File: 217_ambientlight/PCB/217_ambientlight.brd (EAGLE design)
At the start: 27.9 x 39.4 mm, 8 parts

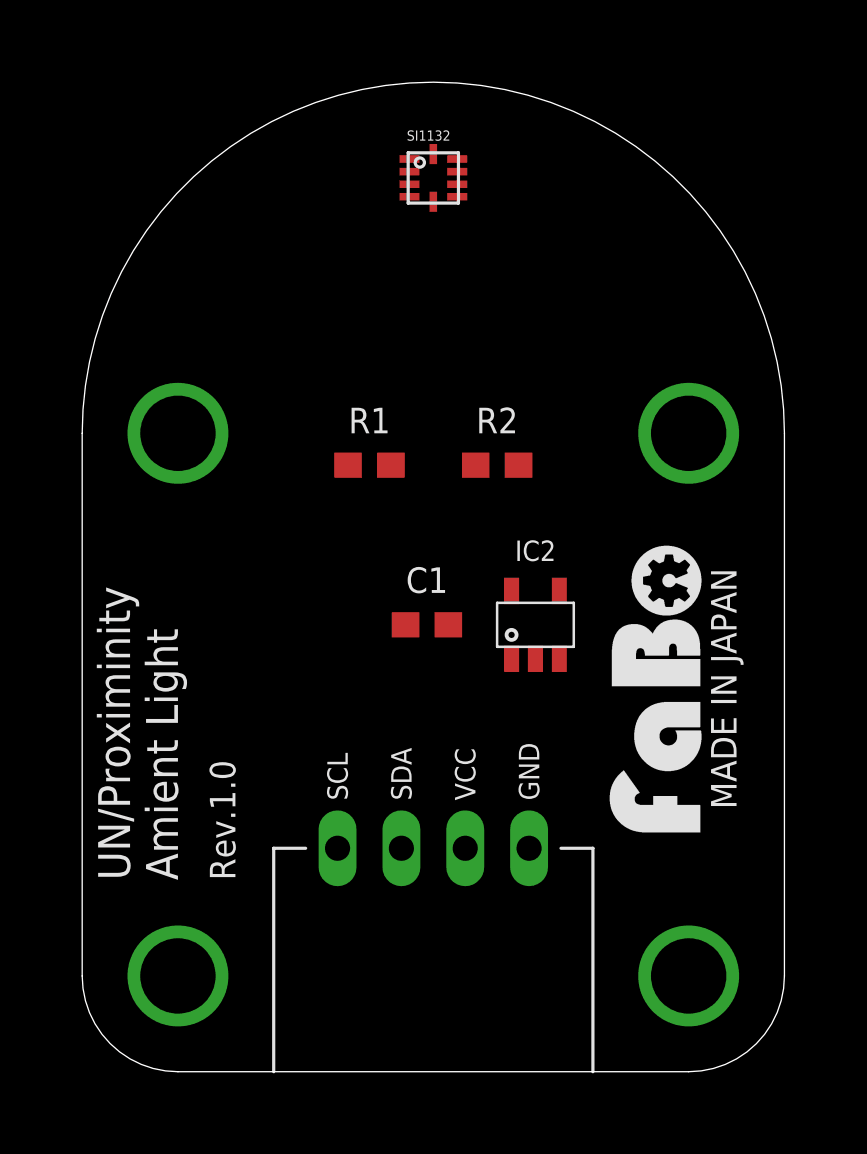
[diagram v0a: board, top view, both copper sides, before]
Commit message: Add new sensors
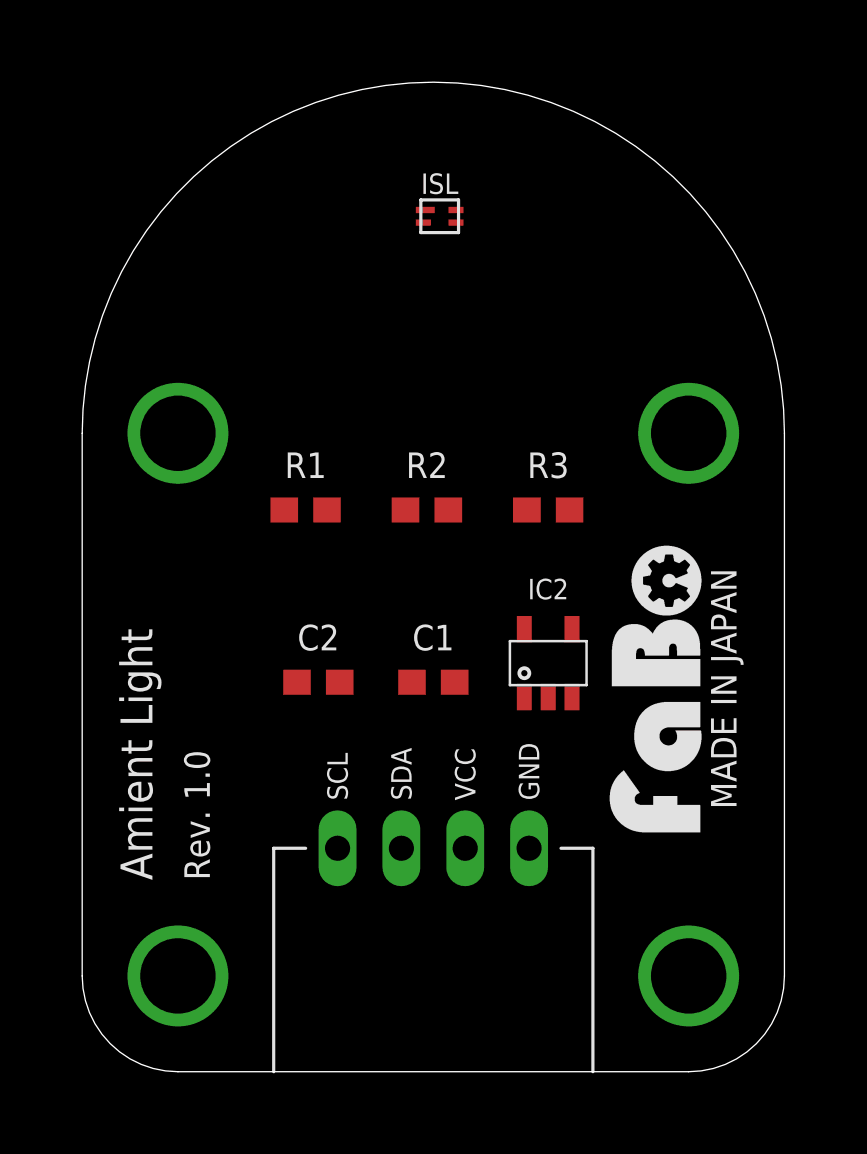
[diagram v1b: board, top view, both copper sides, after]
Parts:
- removed SI1132: SL-SI1132, FaBo-Mems:SILICONLABS-SI1132
- added C2: 1uF, GClue:EIA0603
- added ISL: IN-ISL29034, FaBo-Mems:INTERSIL-ISL29034
- added R3: 100, GClue:EIA0603
- moved R2 3.31 mm to (13.7, 22.4)
- moved R1 3.10 mm to (8.89, 22.4)
- moved C1 2.30 mm to (14.0, 15.5)
- moved IC2 1.61 mm to (18.5, 16.3)
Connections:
- new net N$1: C2.1, ISL.1, R3.1
- net 3V3: now also R3.2; no longer SI1132.3, SI1132.6, SI1132.7, SI1132.9
- net GND: now also C2.2, ISL.2; no longer SI1132.8
- net SCL: now also ISL.3; no longer SI1132.2
- net SDA: now also ISL.4; no longer SI1132.1
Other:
- board text added: "Amient Light"
- board text added: "Rev. 1.0"
- board text removed: "Rev.1.0"
- board text removed: "UN/Proximinity Amient Light"
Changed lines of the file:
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@@
 <plain>
 <text x="26.035" y="15.24" size="1.016" layer="21" font="vector" ratio="12" rot="R90" align="bottom-center">MADE IN JAPAN</text>
-<text x="3.81" y="7.62" size="1.27" layer="21" font="vector" ratio="12" rot="R90">UN/Proximinity
-Amient Light</text>
-<text x="6.096" y="7.62" size="1.016" layer="21" font="vector" ratio="12" rot="R90">Rev.1.0</text>
+<text x="2.794" y="7.62" size="1.27" layer="21" font="vector" ratio="12" rot="R90">Amient Light</text>
+<text x="5.08" y="7.62" size="1.016" layer="21" font="vector" ratio="12" rot="R90">Rev. 1.0</text>
 </plain>
 <attributes>
@@
 <element name="U$3" library="FaBo" package="LOGO_FABO_M" value="" x="24.638" y="15.24" rot="R90"/>
 <element name="U$4" library="GClue" package="LOGO_OSHW_T_M_BOTTOM" value="" x="13.97" y="5.08"/>
-<element name="R1" library="GClue" package="EIA0603" value="4.7k" x="11.43" y="24.13"/>
-<element name="R2" library="GClue" package="EIA0603" value="4.7k" x="16.51" y="24.13"/>
-<element name="SI1132" library="FaBo-Mems" package="SILICONLABS-SI1132" value="SL-SI1132" x="13.97" y="35.56"/>
-<element name="IC2" library="FaBo-Supply" package="TI-LP2985" value="" x="18.034" y="17.78"/>
-<element name="C1" library="GClue" package="EIA0603" value="1uF" x="13.716" y="17.78"/>
+<element name="R1" library="GClue" package="EIA0603" value="4.7k" x="8.89" y="22.352"/>
+<element name="R2" library="GClue" package="EIA0603" value="4.7k" x="13.716" y="22.352"/>
+<element name="ISL" library="FaBo-Mems" package="INTERSIL-ISL29034" value="IN-ISL29034" x="14.224" y="34.036"/>
+<element name="R3" library="GClue" package="EIA0603" value="100" x="18.542" y="22.352"/>
+<element name="C2" library="GClue" package="EIA0603" value="1uF" x="9.398" y="15.494"/>
+<element name="IC2" library="FaBo-Supply" package="TI-LP2985" value="" x="18.542" y="16.256"/>
+<element name="C1" library="GClue" package="EIA0603" value="1uF" x="13.97" y="15.494"/>
 </elements>
 <signals>
@@
 <contactref element="R1" pad="2"/>
 <contactref element="R2" pad="2"/>
-<contactref element="SI1132" pad="3"/>
-<contactref element="SI1132" pad="7"/>
-<contactref element="SI1132" pad="6"/>
-<contactref element="SI1132" pad="9"/>
+<contactref element="R3" pad="2"/>
 <contactref element="IC2" pad="5"/>
 <contactref element="C1" pad="1"/>
-<wire x1="14.92" y1="35.312" x2="14.92" y2="36.312" width="0" layer="19" extent="1-1"/>
-<wire x1="14.92" y1="34.812" x2="14.92" y2="35.312" width="0" layer="19" extent="1-1"/>
-<wire x1="13.02" y1="35.312" x2="14.92" y2="35.312" width="0" layer="19" extent="1-1"/>
-<wire x1="17.36" y1="24.13" x2="14.92" y2="34.812" width="0" layer="19" extent="1-1"/>
-<wire x1="12.28" y1="24.13" x2="17.36" y2="24.13" width="0" layer="19" extent="1-1"/>
-<wire x1="17.084" y1="19.13" x2="12.28" y2="24.13" width="0" layer="19" extent="1-1"/>
-<wire x1="12.866" y1="17.78" x2="17.084" y2="19.13" width="0" layer="19" extent="1-1"/>
+<wire x1="14.566" y1="22.352" x2="19.392" y2="22.352" width="0" layer="19" extent="1-1"/>
+<wire x1="9.74" y1="22.352" x2="14.566" y2="22.352" width="0" layer="19" extent="1-1"/>
+<wire x1="17.592" y1="17.606" x2="19.392" y2="22.352" width="0" layer="19" extent="1-1"/>
+<wire x1="13.12" y1="15.494" x2="17.592" y2="17.606" width="0" layer="19" extent="1-1"/>
 </signal>
 <signal name="GND">
 <contactref element="J1" pad="GND"/>
-<contactref element="SI1132" pad="8"/>
+<contactref element="ISL" pad="2"/>
+<contactref element="C2" pad="2"/>
 <contactref element="IC2" pad="2"/>
 <contactref element="C1" pad="2"/>
-<wire x1="17.78" y1="8.89" x2="14.92" y2="35.812" width="0" layer="19" extent="1-1"/>
-<wire x1="18.034" y1="16.43" x2="17.78" y2="8.89" width="0" layer="19" extent="1-1"/>
-<wire x1="14.566" y1="17.78" x2="18.034" y2="16.43" width="0" layer="19" extent="1-1"/>
+<wire x1="10.248" y1="15.494" x2="13.574" y2="33.786" width="0" layer="19" extent="1-1"/>
+<wire x1="18.542" y1="14.906" x2="10.248" y2="15.494" width="0" layer="19" extent="1-1"/>
+<wire x1="17.78" y1="8.89" x2="18.542" y2="14.906" width="0" layer="19" extent="1-1"/>
+<wire x1="14.82" y1="15.494" x2="17.78" y2="8.89" width="0" layer="19" extent="1-1"/>
 </signal>
 <signal name="SCL">
 <contactref element="J1" pad="SCL"/>
 <contactref element="R2" pad="1"/>
-<contactref element="SI1132" pad="2"/>
-<wire x1="10.16" y1="8.89" x2="15.66" y2="24.13" width="0" layer="19" extent="1-1"/>
-<wire x1="13.02" y1="35.812" x2="10.16" y2="8.89" width="0" layer="19" extent="1-1"/>
+<contactref element="ISL" pad="3"/>
+<wire x1="10.16" y1="8.89" x2="12.866" y2="22.352" width="0" layer="19" extent="1-1"/>
+<wire x1="14.874" y1="33.786" x2="10.16" y2="8.89" width="0" layer="19" extent="1-1"/>
 </signal>
 <signal name="SDA">
 <contactref element="J1" pad="SDA"/>
 <contactref element="R1" pad="1"/>
-<contactref element="SI1132" pad="1"/>
-<wire x1="12.7" y1="8.89" x2="10.58" y2="24.13" width="0" layer="19" extent="1-1"/>
-<wire x1="13.02" y1="36.312" x2="12.7" y2="8.89" width="0" layer="19" extent="1-1"/>
+<contactref element="ISL" pad="4"/>
+<wire x1="12.7" y1="8.89" x2="8.04" y2="22.352" width="0" layer="19" extent="1-1"/>
+<wire x1="14.874" y1="34.286" x2="12.7" y2="8.89" width="0" layer="19" extent="1-1"/>
+</signal>
+<signal name="N$1">
+<contactref element="ISL" pad="1"/>
+<contactref element="R3" pad="1"/>
+<contactref element="C2" pad="1"/>
+<wire x1="17.692" y1="22.352" x2="8.548" y2="15.494" width="0" layer="19" extent="1-1"/>
+<wire x1="13.649" y1="34.286" x2="17.692" y2="22.352" width="0" layer="19" extent="1-1"/>
 </signal>
 <signal name="5V">
@@
 <contactref element="IC2" pad="1"/>
 <contactref element="J1" pad="VCC"/>
-<wire x1="18.984" y1="16.43" x2="15.24" y2="8.89" width="0" layer="19" extent="1-1"/>
-<wire x1="17.084" y1="16.43" x2="18.984" y2="16.43" width="0" layer="19" extent="1-1"/>
+<wire x1="19.492" y1="14.906" x2="15.24" y2="8.89" width="0" layer="19" extent="1-1"/>
+<wire x1="17.592" y1="14.906" x2="19.492" y2="14.906" width="0" layer="19" extent="1-1"/>
 </signal>
 </signals>
@@
 </board>
 </drawing>
-<compatibility>
-<note version="6.3" minversion="6.2.2" severity="warning">
-Since Version 6.2.2 text objects can contain more than one line,
-which will not be processed correctly with this version.
-</note>
-</compatibility>
 </eagle>

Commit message: fix 206_uv fix 217_ambientlight
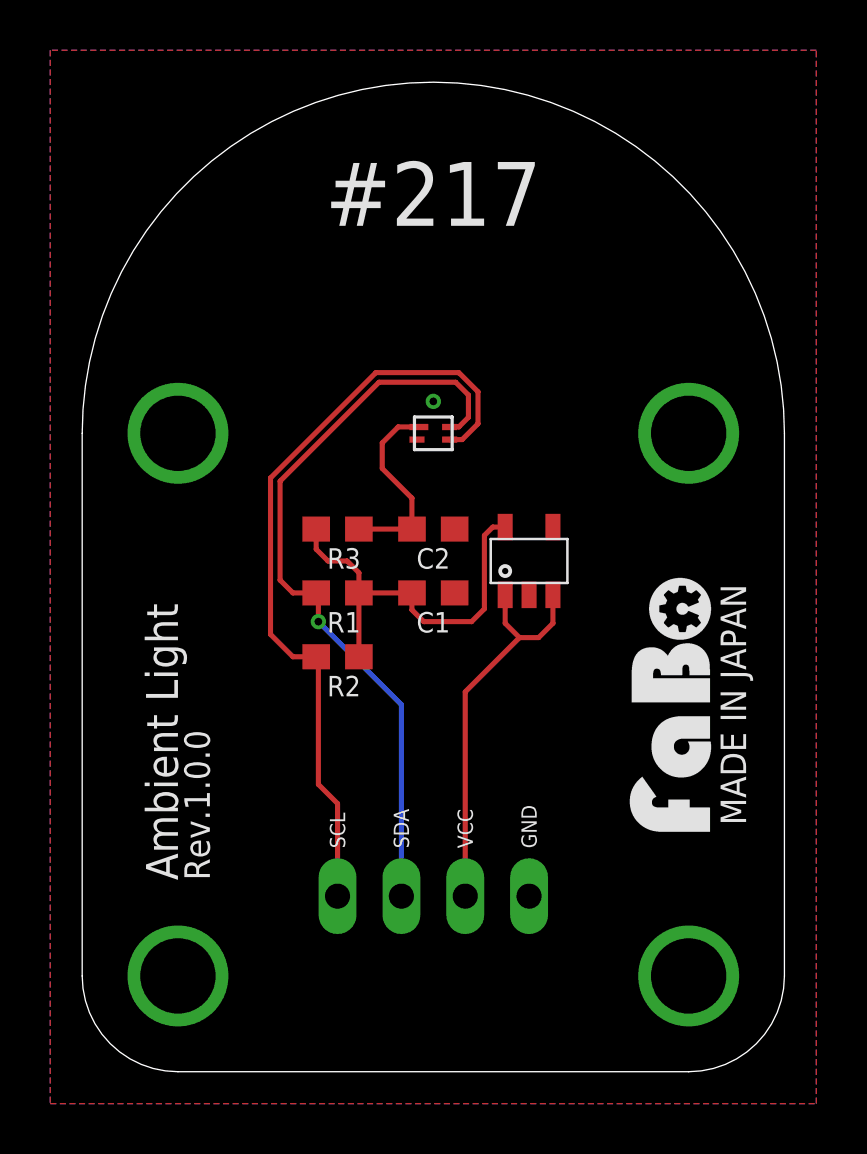
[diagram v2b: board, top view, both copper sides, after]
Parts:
- removed ISL: IN-ISL29034, FaBo-Mems:INTERSIL-ISL29034
- removed U$4: (no value), GClue:LOGO_OSHW_T_M_BOTTOM
- added IC1: (no value), FaBo-Supply:TI-LP2985
- added U$2: (no value), FaBo-etc:LOGO_OSHW_T_MS_BOTTOM
- C1, C2: device GClue:EIA0603 -> FaBo-Capacitor:0603
- IC2: value (none) -> IN-ISL29034; device FaBo-Supply:TI-LP2985 -> FaBo-Mems:INTERSIL-ISL29034
- J1: device GClue:BRICK_I2C -> FaBo-Template:FABO_BRICK_I2C
- R1, R2, R3: device GClue:EIA0603 -> FaBo-Resistors:0603
- U$3: device FaBo:LOGO_FABO_M -> FaBo-etc:LOGO_FABO_MS
- moved IC2 10.2 mm to (14.0, 25.4)
- moved R3 8.42 mm to (10.2, 21.6), turned to 180 degrees
- moved C2 7.62 mm to (14.0, 21.6), turned to 180 degrees
- moved R2 6.84 mm to (10.2, 16.5)
- moved C1 3.56 mm to (14.0, 19.1), turned to 180 degrees
- moved R1 3.54 mm to (10.2, 19.1)
- moved U$3 0.99 mm to (25.4, 14.6)
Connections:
- removed net N$1: C2.1, ISL.1, R3.1
- new net VCC: C2.2, IC2.1, R3.1
- net 3V3: now also C1.2, IC1.5; no longer C1.1, IC2.5
- net 5V: now also IC1.1, IC1.3; no longer IC2.1, IC2.3
- net GND: now also C1.1, C2.1, IC1.2; no longer C1.2, C2.2, ISL.2
- net SCL: now also IC2.3; no longer ISL.3
- net SDA: now also IC2.4; no longer ISL.4
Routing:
- net SCL: track 0.00 -> 31.3 mm
- net SDA: track 0.00 -> 30.2 mm, vias 0 -> 1
- net 3V3: track 0.00 -> 16.2 mm
- net 5V: track 0.00 -> 15.8 mm
- net VCC: track 0.00 -> 7.75 mm
- added copper zone on layer 1, net GND
- added copper zone on layer 16, net GND
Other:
- board text added: "#217"
- board text added: "Ambient Light"
- board text added: "Rev.1.0.0"
- board text removed: "Amient Light"
- board text removed: "Rev. 1.0"

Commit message: change dru seeed
212 is draft
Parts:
- removed R3: 100, FaBo-Resistors:0603
- added C3: 1uF, FaBo-Capacitor:0603
- added IC3: (no value), FaBo-Mems:INTERSIL-ISL29034
- added TP1, TP2: (no value), FaBo-Supply:TP-10
- C2: value 1uF -> 0.1uF
- IC2: value IN-ISL29034 -> (none); device FaBo-Mems:INTERSIL-ISL29034 -> FaBo-LevelTranslator:X2SON
- R1: value 4.7k -> 200k
- R2: value 4.7k -> 100
- U$2: device FaBo-etc:LOGO_OSHW_T_MS_BOTTOM -> FaBo-etc:LOGO_OSHW_M_BOTTOM
- moved IC2 8.98 mm to (7.62, 19.1), turned to 180 degrees
- moved R2 7.73 mm to (11.4, 24.1), turned to 180 degrees
- moved C1 3.59 mm to (16.5, 21.6)
- moved C2 3.59 mm to (11.4, 19.1)
- moved IC1 2.84 mm to (16.5, 17.8)
- moved R1 2.84 mm to (11.4, 16.5)
- moved U$2 0.38 mm to (14.0, 3.17)
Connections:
- new net N$1: C2.2, IC2.7, IC2.8, R1.1
- new net SCL_HV: IC2.6, J1.SCL
- new net SDA_HV: IC2.5, J1.SDA
- net 3V3: now also IC2.2; no longer R1.2, R3.2
- net 5V: now also R1.2
- net GND: now also C3.1, IC2.1, IC3.2; no longer IC2.2
- net SCL: now also IC3.3, TP2.1; no longer J1.SCL, R2.1
- net SDA: now also IC3.4, TP1.1; no longer J1.SDA, R1.1
- net VCC: now also C3.2, IC3.1, R2.1; no longer C2.2, IC2.1, R3.1
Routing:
- net SDA: track 30.2 -> 11.8 mm, vias 1 -> 2
- net SCL: track 31.3 -> 13.3 mm, vias 0 -> 1
- net SDA_HV: track 0.00 -> 14.6 mm, vias 0 -> 1
- net SCL_HV: track 0.00 -> 11.9 mm
- net N$1: track 0.00 -> 5.49 mm
- net 3V3: track 16.2 -> 14.7 mm
- net VCC: track 7.75 -> 6.46 mm
- net 5V: track 15.8 -> 14.9 mm
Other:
- board text added: "Rev.1.0.1"
- board text removed: "Rev.1.0.0"

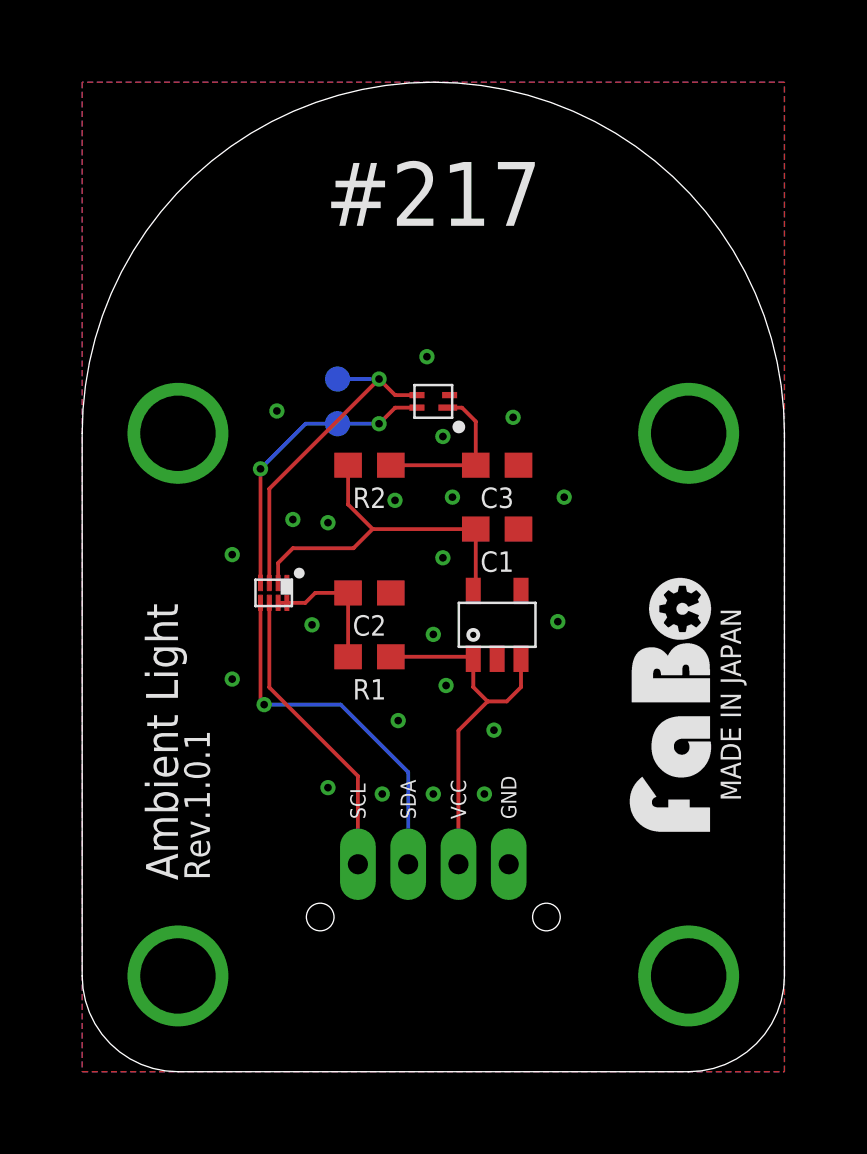
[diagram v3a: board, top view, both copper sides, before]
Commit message: change 217 packages
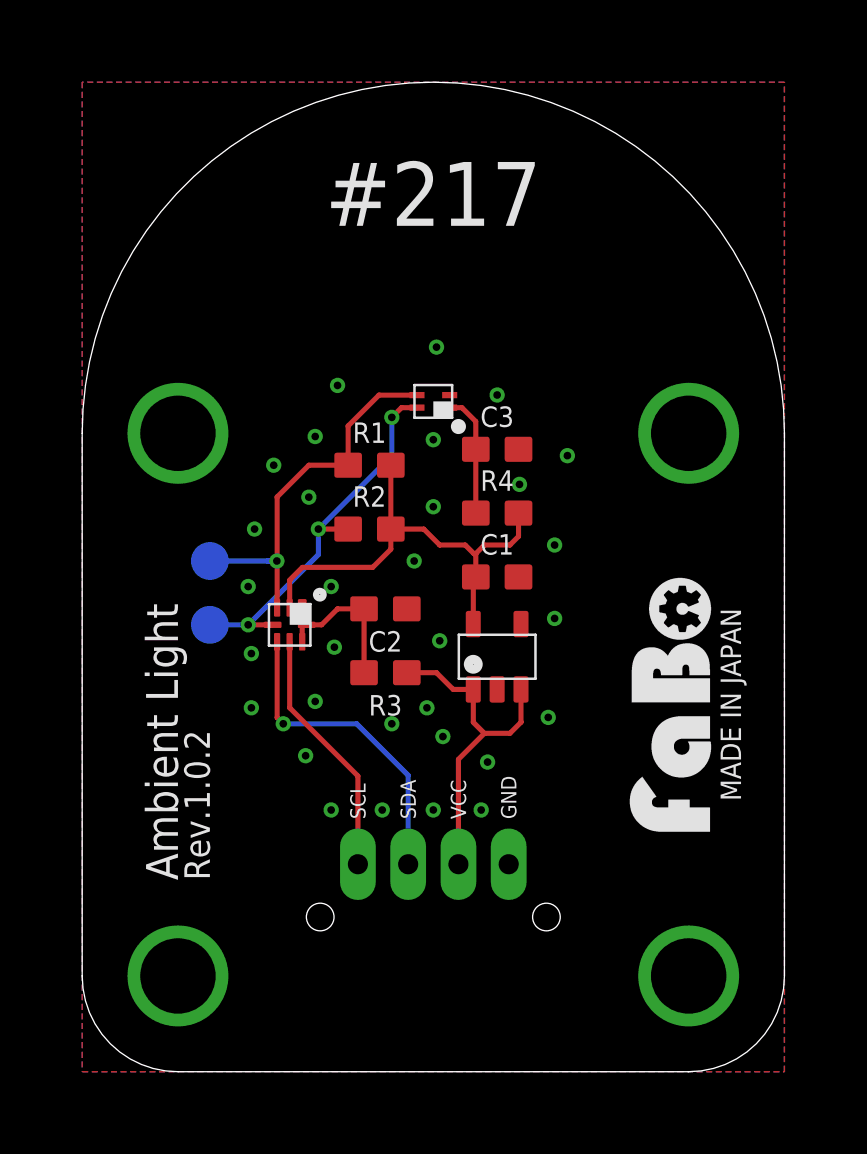
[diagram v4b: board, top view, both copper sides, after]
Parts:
- added R3: 200k, FaBo-Resistors:0603
- added R4: 100, FaBo-Resistors:0603
- IC1: device FaBo-Supply:TI-LP2985 -> FaBo-Mems:INTERSIL-ISL29034
- IC2: device FaBo-LevelTranslator:X2SON -> FaBo-Supply:SOT-23-5
- IC3: device FaBo-Mems:INTERSIL-ISL29034 -> FaBo-LevelTranslator:XQFN8
- R1: value 200k -> 4.7k
- R2: value 100 -> 4.7k
- TP1, TP2: device FaBo-Supply:TP-10 -> FaBo-Supply:TP-15
- moved IC3 10.6 mm to (8.26, 17.8), turned to 270 degrees
- moved TP1 9.48 mm to (5.08, 17.8)
- moved IC1 9.25 mm to (14.0, 26.7), turned to 180 degrees
- moved IC2 9.25 mm to (16.5, 16.5), turned to 0 degrees
- moved TP2 8.84 mm to (5.08, 20.3)
- moved R1 7.62 mm to (11.4, 24.1)
- moved R2 2.54 mm to (11.4, 21.6), turned to 0 degrees
- moved C1 1.91 mm to (16.5, 19.7)
- moved C2 0.90 mm to (12.1, 18.4)
- moved C3 0.64 mm to (16.5, 24.8)
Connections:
- removed net N$1: C2.2, IC2.7, IC2.8, R1.1
- new net N$2: C2.2, IC3.7, IC3.8, R3.1
- net 3V3: now also IC2.5, IC3.2, R1.2, R4.2; no longer IC1.5, IC2.2
- net 5V: now also IC2.1, IC2.3, R3.2; no longer IC1.1, IC1.3, R1.2
- net GND: now also IC2.2, IC3.1; no longer IC2.1, IC3.2
- net SCL: now also IC1.3, R1.1; no longer IC2.3
- net SCL_HV: now also IC3.6; no longer IC2.6
- net SDA: now also IC1.4, R2.1; no longer IC2.4
- net SDA_HV: now also IC3.5; no longer IC2.5
- net VCC: now also IC1.1, R4.1; no longer IC3.1, R2.1
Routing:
- net N$2: track 0.00 -> 5.94 mm
- net N$1: track 5.49 -> 0.00 mm
- net 3V3: track 14.7 -> 18.5 mm
- net SDA: track 11.8 -> 15.5 mm, vias 2 -> 3
- net SCL: track 13.3 -> 15.6 mm
- net SDA_HV: track 14.6 -> 12.7 mm
- net SCL_HV: track 11.9 -> 9.97 mm
- net VCC: track 6.46 -> 4.99 mm
- net 5V: track 14.9 -> 13.4 mm
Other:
- board text added: "Rev.1.0.2"
- board text removed: "Rev.1.0.1"
